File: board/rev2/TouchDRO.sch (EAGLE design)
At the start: 24 parts, among them U2 VREG_33, U3 VREG_5

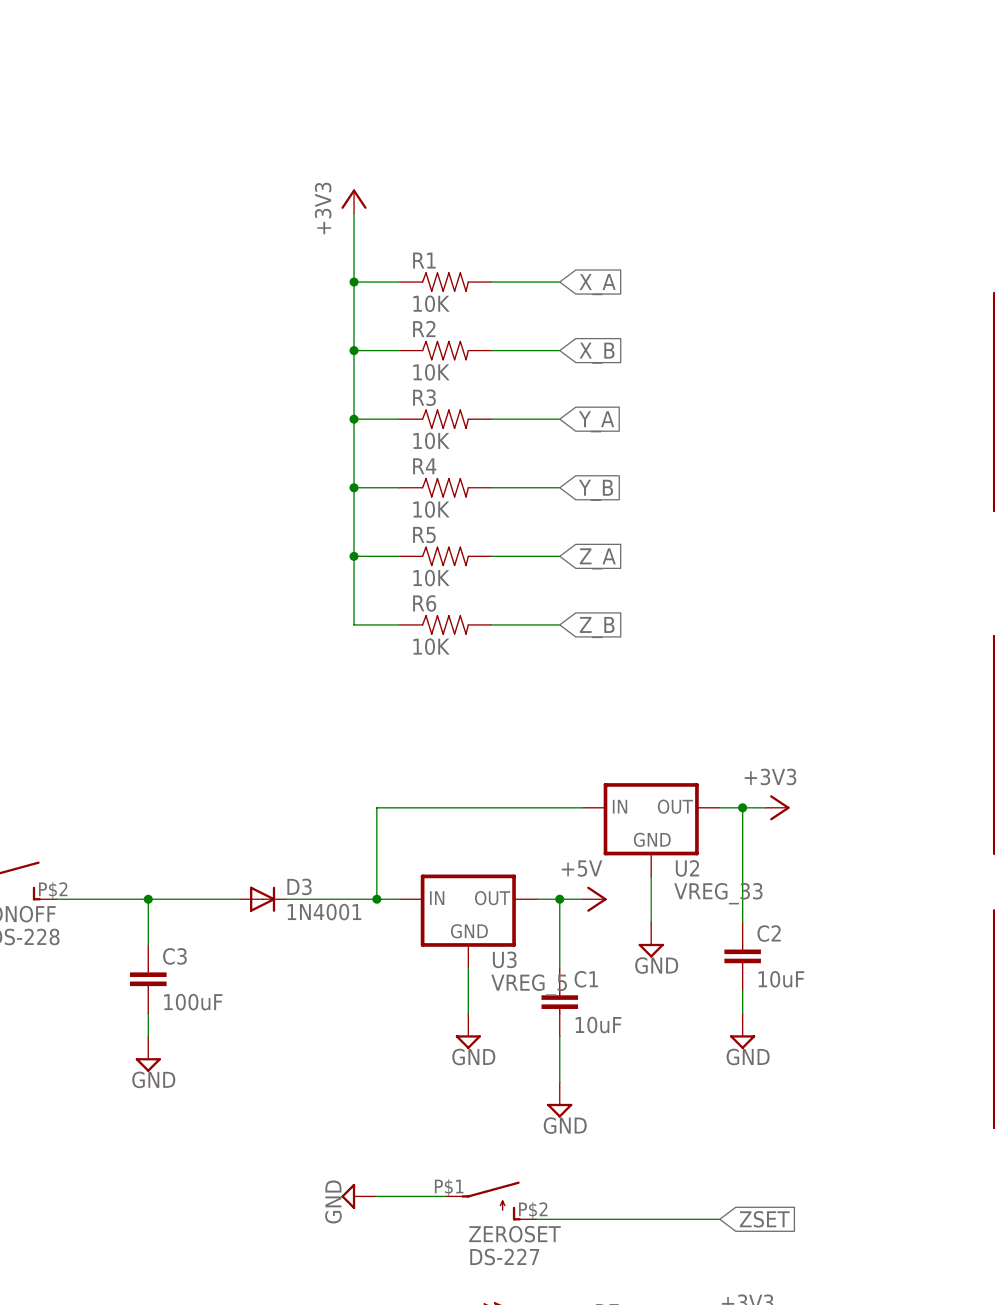
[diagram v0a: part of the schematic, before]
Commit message: adding additional caps to voltage regulator outputs
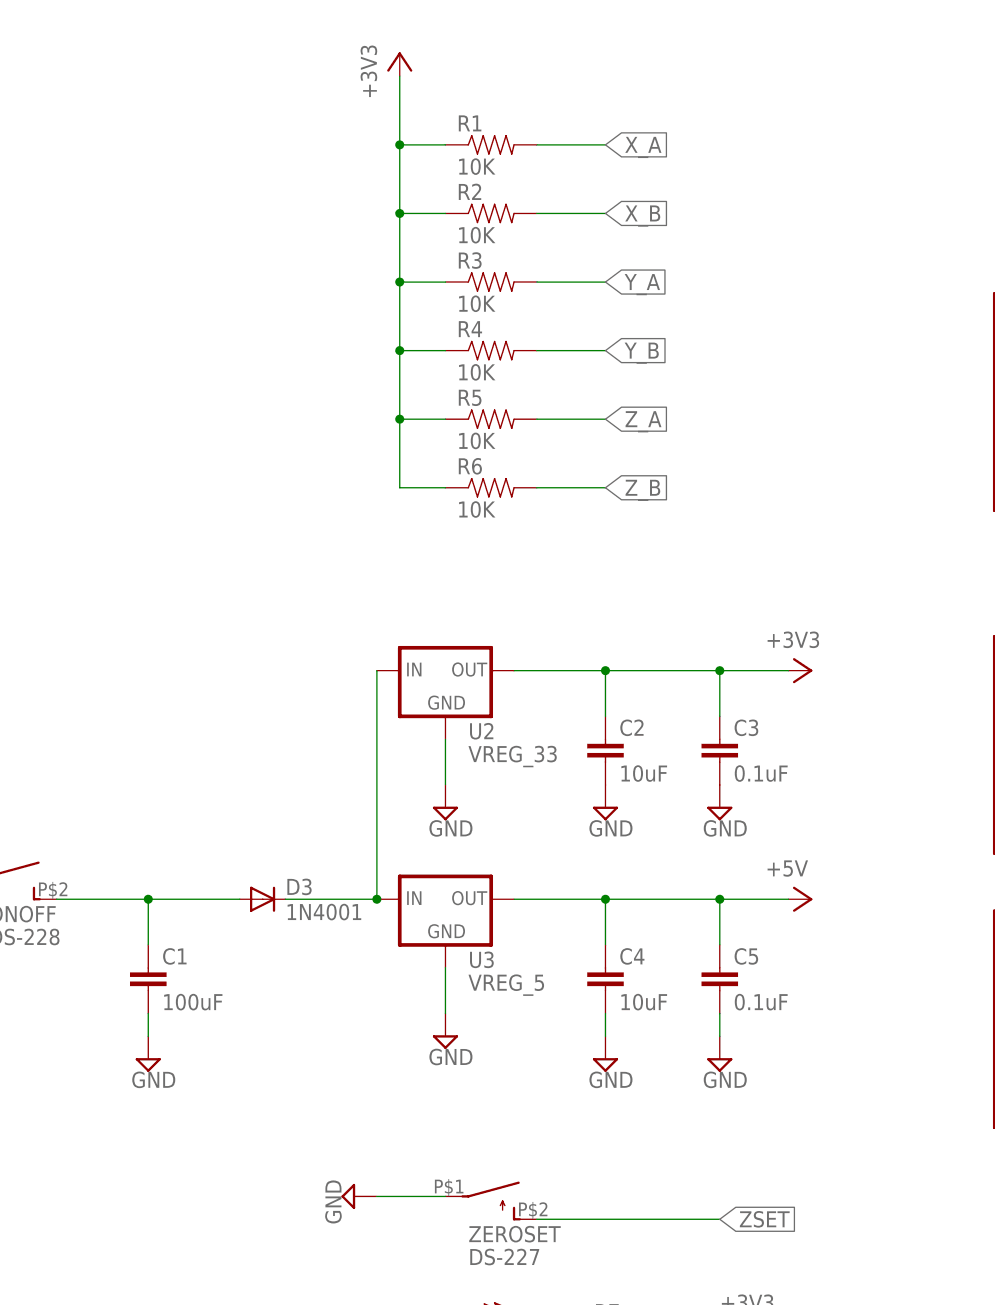
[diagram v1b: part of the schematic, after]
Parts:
- added C4: 10uF, SparkFun-Passives:CAPEZ
- added C5: 0.1uF, SparkFun-Passives:CAPEZ
- C1: value 10uF -> 100uF
- C3: value 100uF -> 0.1uF
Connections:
- net +3V3: now also C3.1
- net +5V: now also C4.1, C5.1; no longer C1.1
- net GND: now also C4.2, C5.2
- net ONOFF: now also C1.1; no longer C3.1
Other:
- moved on the sheet: C1, C2, C3, R1, R2, R3, R4, R5, R6, U2, U3

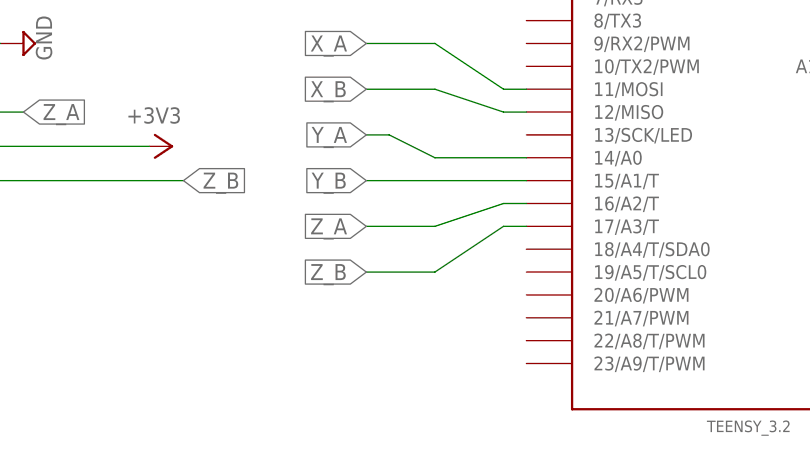
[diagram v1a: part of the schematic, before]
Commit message: rerouting z-axis signals to new pins
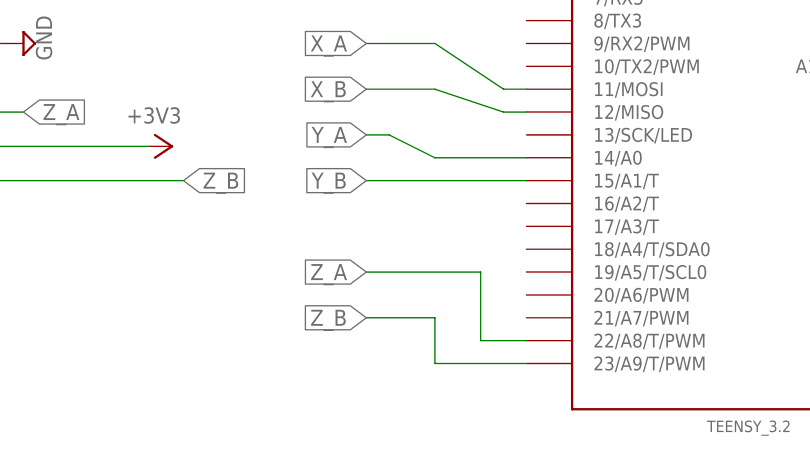
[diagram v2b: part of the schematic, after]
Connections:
- net Z_A: now also U$1.22/A8/T/PWM; no longer U$1.16/A2/T
- net Z_B: now also U$1.23/A9/T/PWM; no longer U$1.17/A3/T
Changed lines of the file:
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@@
 </segment>
 <segment>
-<pinref part="U$1" gate="G$1" pin="16/A2/T"/>
-<wire x1="55.88" y1="-30.48" x2="53.34" y2="-30.48" width="0.1524" layer="91"/>
-<wire x1="53.34" y1="-30.48" x2="45.72" y2="-33.02" width="0.1524" layer="91"/>
-<wire x1="45.72" y1="-33.02" x2="38.1" y2="-33.02" width="0.1524" layer="91"/>
-<label x="38.1" y="-33.02" size="1.778" layer="95" rot="R180" xref="yes"/>
+<label x="38.1" y="-38.1" size="1.778" layer="95" rot="R180" xref="yes"/>
+<wire x1="38.1" y1="-38.1" x2="50.8" y2="-38.1" width="0.1524" layer="91"/>
+<wire x1="50.8" y1="-38.1" x2="50.8" y2="-45.72" width="0.1524" layer="91"/>
+<pinref part="U$1" gate="G$1" pin="22/A8/T/PWM"/>
+<wire x1="50.8" y1="-45.72" x2="55.88" y2="-45.72" width="0.1524" layer="91"/>
 </segment>
 <segment>
@@
 </segment>
 <segment>
-<pinref part="U$1" gate="G$1" pin="17/A3/T"/>
-<wire x1="55.88" y1="-33.02" x2="53.34" y2="-33.02" width="0.1524" layer="91"/>
-<wire x1="53.34" y1="-33.02" x2="45.72" y2="-38.1" width="0.1524" layer="91"/>
-<wire x1="45.72" y1="-38.1" x2="38.1" y2="-38.1" width="0.1524" layer="91"/>
-<label x="38.1" y="-38.1" size="1.778" layer="95" rot="R180" xref="yes"/>
+<label x="38.1" y="-43.18" size="1.778" layer="95" rot="R180" xref="yes"/>
+<wire x1="38.1" y1="-43.18" x2="45.72" y2="-43.18" width="0.1524" layer="91"/>
+<wire x1="45.72" y1="-43.18" x2="45.72" y2="-48.26" width="0.1524" layer="91"/>
+<pinref part="U$1" gate="G$1" pin="23/A9/T/PWM"/>
+<wire x1="45.72" y1="-48.26" x2="55.88" y2="-48.26" width="0.1524" layer="91"/>
 </segment>
 <segment>

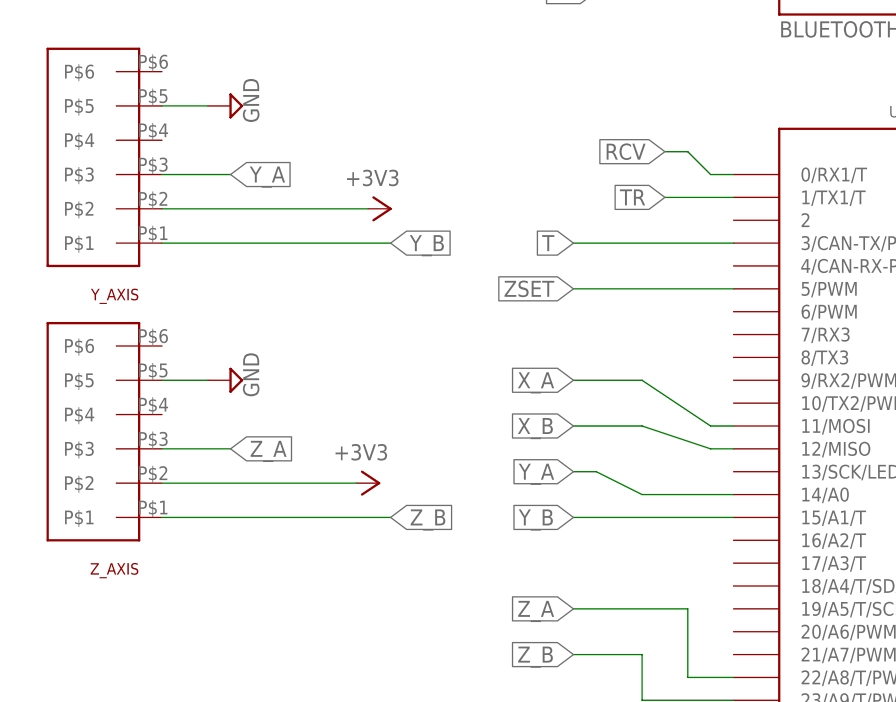
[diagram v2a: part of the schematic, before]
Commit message: added dual routing of tach signal to handle 3.2 and LC versions
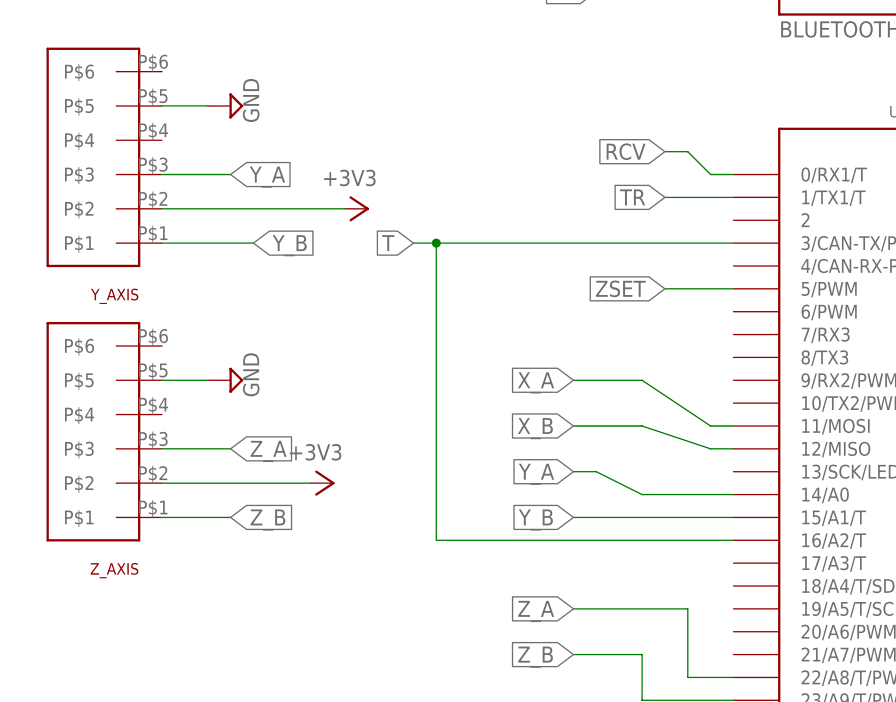
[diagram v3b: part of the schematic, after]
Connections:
- net T: now also U$1.16/A2/T
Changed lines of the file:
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@@
 <instance part="+3V5" gate="G$1" x="18.796" y="44.45" rot="R270"/>
 <instance part="+3V6" gate="G$1" x="15.24" y="78.74" rot="R270"/>
-<instance part="+3V8" gate="G$1" x="16.51" y="-24.13" rot="R270"/>
-<instance part="+3V9" gate="G$1" x="17.78" y="6.35" rot="R270"/>
+<instance part="+3V8" gate="G$1" x="11.43" y="-24.13" rot="R270"/>
+<instance part="+3V9" gate="G$1" x="15.24" y="6.35" rot="R270"/>
 <instance part="C2" gate="G$1" x="-63.5" y="10.16"/>
 <instance part="SUPPLY1" gate="GND" x="-63.5" y="5.08"/>
@@
 <segment>
 <pinref part="Z_AXIS" gate="G$1" pin="P$1"/>
-<wire x1="-7.62" y1="-27.94" x2="17.78" y2="-27.94" width="0.1524" layer="91"/>
-<label x="17.78" y="-27.94" size="1.778" layer="95" xref="yes"/>
+<wire x1="-7.62" y1="-27.94" x2="0" y2="-27.94" width="0.1524" layer="91"/>
+<label x="0" y="-27.94" size="1.778" layer="95" xref="yes"/>
 </segment>
 <segment>
@@
 <segment>
 <pinref part="Y_AXIS" gate="G$1" pin="P$1"/>
-<wire x1="-7.62" y1="2.54" x2="17.78" y2="2.54" width="0.1524" layer="91"/>
-<label x="17.78" y="2.54" size="1.778" layer="95" xref="yes"/>
+<wire x1="-7.62" y1="2.54" x2="2.54" y2="2.54" width="0.1524" layer="91"/>
+<label x="2.54" y="2.54" size="1.778" layer="95" xref="yes"/>
 </segment>
 <segment>
@@
 <segment>
 <pinref part="U$1" gate="G$1" pin="3/CAN-TX/PWM"/>
-<wire x1="55.88" y1="2.54" x2="38.1" y2="2.54" width="0.1524" layer="91"/>
-<label x="38.1" y="2.54" size="1.778" layer="95" rot="R180" xref="yes"/>
+<wire x1="55.88" y1="2.54" x2="22.86" y2="2.54" width="0.1524" layer="91"/>
+<label x="20.32" y="2.54" size="1.778" layer="95" rot="R180" xref="yes"/>
+<wire x1="22.86" y1="2.54" x2="20.32" y2="2.54" width="0.1524" layer="91"/>
+<wire x1="22.86" y1="2.54" x2="22.86" y2="-30.48" width="0.1524" layer="91"/>
+<junction x="22.86" y="2.54"/>
+<pinref part="U$1" gate="G$1" pin="16/A2/T"/>
+<wire x1="22.86" y1="-30.48" x2="55.88" y2="-30.48" width="0.1524" layer="91"/>
 </segment>
 </net>
@@
 <segment>
 <pinref part="Y_AXIS" gate="G$1" pin="P$2"/>
-<wire x1="-7.62" y1="6.35" x2="15.24" y2="6.35" width="0.1524" layer="91"/>
+<wire x1="-7.62" y1="6.35" x2="12.7" y2="6.35" width="0.1524" layer="91"/>
 <pinref part="+3V9" gate="G$1" pin="+3V3"/>
 </segment>
 <segment>
 <pinref part="Z_AXIS" gate="G$1" pin="P$2"/>
-<wire x1="-7.62" y1="-24.13" x2="13.97" y2="-24.13" width="0.1524" layer="91"/>
+<wire x1="-7.62" y1="-24.13" x2="8.89" y2="-24.13" width="0.1524" layer="91"/>
 <pinref part="+3V8" gate="G$1" pin="+3V3"/>
 </segment>
@@
 <segment>
 <pinref part="U$1" gate="G$1" pin="5/PWM"/>
-<wire x1="55.88" y1="-2.54" x2="38.1" y2="-2.54" width="0.1524" layer="91"/>
-<label x="38.1" y="-2.54" size="1.778" layer="95" rot="R180" xref="yes"/>
-</segment>
-<segment>
+<wire x1="55.88" y1="-2.54" x2="48.26" y2="-2.54" width="0.1524" layer="91"/>
+<label x="48.26" y="-2.54" size="1.778" layer="95" rot="R180" xref="yes"/>
+</segment>
+<segment>

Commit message: added bluetooth KEY signal. changed pins in microcontroller code to match new design
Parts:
- renumbered LED1 to PWRLED
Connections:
- new net KEY: J_BT_BOARD_1.KEY, U$1.2
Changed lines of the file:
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@@
 <?xml version="1.0" encoding="utf-8"?>
 <!DOCTYPE eagle SYSTEM "eagle.dtd">
-<eagle version="7.3.0">
+<eagle version="7.5.0">
 <drawing>
 <settings>
@@
 <part name="U2" library="regulators" deviceset="VREG_33" device=""/>
 <part name="U3" library="regulators" deviceset="VREG_5" device=""/>
-<part name="LED1" library="led" deviceset="LED" device="3MM"/>
+<part name="PWRLED" library="led" deviceset="LED" device="3MM"/>
 <part name="SUPPLY4" library="supply2" deviceset="GND" device=""/>
 <part name="+3V7" library="supply1" deviceset="+3V3" device=""/>
@@
 <instance part="U2" gate="G$1" x="-81.28" y="20.32"/>
 <instance part="U3" gate="G$1" x="-81.28" y="-5.08"/>
-<instance part="LED1" gate="G$1" x="-73.66" y="-53.34" rot="R270"/>
+<instance part="PWRLED" gate="G$1" x="-73.66" y="-53.34" rot="R270"/>
 <instance part="SUPPLY4" gate="GND" x="-91.44" y="-53.34" rot="R270"/>
 <instance part="+3V7" gate="G$1" x="-45.72" y="-53.34" rot="R270"/>
@@
 <segment>
 <pinref part="SUPPLY4" gate="GND" pin="GND"/>
-<pinref part="LED1" gate="G$1" pin="C"/>
+<pinref part="PWRLED" gate="G$1" pin="C"/>
 <wire x1="-88.9" y1="-53.34" x2="-78.74" y2="-53.34" width="0.1524" layer="91"/>
 </segment>
@@
 <segment>
 <pinref part="U$1" gate="G$1" pin="0/RX1/T"/>
-<label x="48.26" y="12.7" size="1.778" layer="95" rot="R180" xref="yes"/>
+<label x="43.18" y="15.24" size="1.778" layer="95" rot="R180" xref="yes"/>
 <wire x1="55.88" y1="10.16" x2="53.34" y2="10.16" width="0.1524" layer="91"/>
-<wire x1="53.34" y1="10.16" x2="50.8" y2="12.7" width="0.1524" layer="91"/>
-<wire x1="50.8" y1="12.7" x2="48.26" y2="12.7" width="0.1524" layer="91"/>
+<wire x1="53.34" y1="10.16" x2="48.26" y2="15.24" width="0.1524" layer="91"/>
+<wire x1="48.26" y1="15.24" x2="43.18" y2="15.24" width="0.1524" layer="91"/>
 </segment>
 <segment>
@@
 <segment>
 <pinref part="U$1" gate="G$1" pin="1/TX1/T"/>
-<label x="48.26" y="7.62" size="1.778" layer="95" rot="R180" xref="yes"/>
-<wire x1="48.26" y1="7.62" x2="55.88" y2="7.62" width="0.1524" layer="91"/>
+<label x="43.18" y="10.16" size="1.778" layer="95" rot="R180" xref="yes"/>
+<wire x1="43.18" y1="10.16" x2="50.8" y2="10.16" width="0.1524" layer="91"/>
+<wire x1="50.8" y1="10.16" x2="53.34" y2="7.62" width="0.1524" layer="91"/>
+<wire x1="53.34" y1="7.62" x2="55.88" y2="7.62" width="0.1524" layer="91"/>
 </segment>
 </net>
@@
 </segment>
 <segment>
-<label x="38.1" y="-38.1" size="1.778" layer="95" rot="R180" xref="yes"/>
-<wire x1="38.1" y1="-38.1" x2="50.8" y2="-38.1" width="0.1524" layer="91"/>
-<wire x1="50.8" y1="-38.1" x2="50.8" y2="-45.72" width="0.1524" layer="91"/>
+<label x="38.1" y="-43.18" size="1.778" layer="95" rot="R180" xref="yes"/>
 <pinref part="U$1" gate="G$1" pin="22/A8/T/PWM"/>
 <wire x1="50.8" y1="-45.72" x2="55.88" y2="-45.72" width="0.1524" layer="91"/>
+<wire x1="50.8" y1="-45.72" x2="45.72" y2="-43.18" width="0.1524" layer="91"/>
+<wire x1="45.72" y1="-43.18" x2="38.1" y2="-43.18" width="0.1524" layer="91"/>
 </segment>
 <segment>
@@
 </segment>
 <segment>
-<label x="38.1" y="-43.18" size="1.778" layer="95" rot="R180" xref="yes"/>
-<wire x1="38.1" y1="-43.18" x2="45.72" y2="-43.18" width="0.1524" layer="91"/>
-<wire x1="45.72" y1="-43.18" x2="45.72" y2="-48.26" width="0.1524" layer="91"/>
+<label x="38.1" y="-48.26" size="1.778" layer="95" rot="R180" xref="yes"/>
 <pinref part="U$1" gate="G$1" pin="23/A9/T/PWM"/>
-<wire x1="45.72" y1="-48.26" x2="55.88" y2="-48.26" width="0.1524" layer="91"/>
+<wire x1="38.1" y1="-48.26" x2="55.88" y2="-48.26" width="0.1524" layer="91"/>
 </segment>
 <segment>
@@
 <net name="N$1" class="0">
 <segment>
-<pinref part="LED1" gate="G$1" pin="A"/>
+<pinref part="PWRLED" gate="G$1" pin="A"/>
 <pinref part="R7" gate="G$1" pin="1"/>
 <wire x1="-71.12" y1="-53.34" x2="-66.04" y2="-53.34" width="0.1524" layer="91"/>
 </segment>
 </net>
+<net name="KEY" class="0">
+<segment>
+<pinref part="J_BT_BOARD_1" gate="J_BT_BOARD" pin="KEY"/>
+<wire x1="81.28" y1="43.18" x2="91.44" y2="43.18" width="0.1524" layer="91"/>
+<label x="91.44" y="43.18" size="1.778" layer="95" xref="yes"/>
+</segment>
+<segment>
+<pinref part="U$1" gate="G$1" pin="2"/>
+<wire x1="55.88" y1="5.08" x2="43.18" y2="5.08" width="0.1524" layer="91"/>
+<label x="43.18" y="5.08" size="1.778" layer="95" rot="R180" xref="yes"/>
+</segment>
+</net>

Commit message: modified rev2 board to use multifrequencymeasure library (which allows to specify of pin)
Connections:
- net T: now also U$1.6/PWM; no longer U$1.16/A2/T, U$1.3/CAN-TX/PWM
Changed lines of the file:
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@@
 </segment>
 <segment>
-<pinref part="U$1" gate="G$1" pin="3/CAN-TX/PWM"/>
-<wire x1="55.88" y1="2.54" x2="22.86" y2="2.54" width="0.1524" layer="91"/>
-<label x="20.32" y="2.54" size="1.778" layer="95" rot="R180" xref="yes"/>
-<wire x1="22.86" y1="2.54" x2="20.32" y2="2.54" width="0.1524" layer="91"/>
-<wire x1="22.86" y1="2.54" x2="22.86" y2="-30.48" width="0.1524" layer="91"/>
-<junction x="22.86" y="2.54"/>
-<pinref part="U$1" gate="G$1" pin="16/A2/T"/>
-<wire x1="22.86" y1="-30.48" x2="55.88" y2="-30.48" width="0.1524" layer="91"/>
+<label x="48.26" y="-7.62" size="1.778" layer="95" rot="R180" xref="yes"/>
+<wire x1="48.26" y1="-7.62" x2="50.8" y2="-7.62" width="0.1524" layer="91"/>
+<wire x1="50.8" y1="-7.62" x2="53.34" y2="-5.08" width="0.1524" layer="91"/>
+<pinref part="U$1" gate="G$1" pin="6/PWM"/>
+<wire x1="53.34" y1="-5.08" x2="55.88" y2="-5.08" width="0.1524" layer="91"/>
 </segment>
 </net>
